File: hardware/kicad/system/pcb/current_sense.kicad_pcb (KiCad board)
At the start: 2 copper layers, 134 x 58 mm, 17 parts, among them J1 kanal 1 retur, J2 kanal 2 retur, J3 kanal 3 retur, J4 Arduino, U1 LM358, U2 LM358

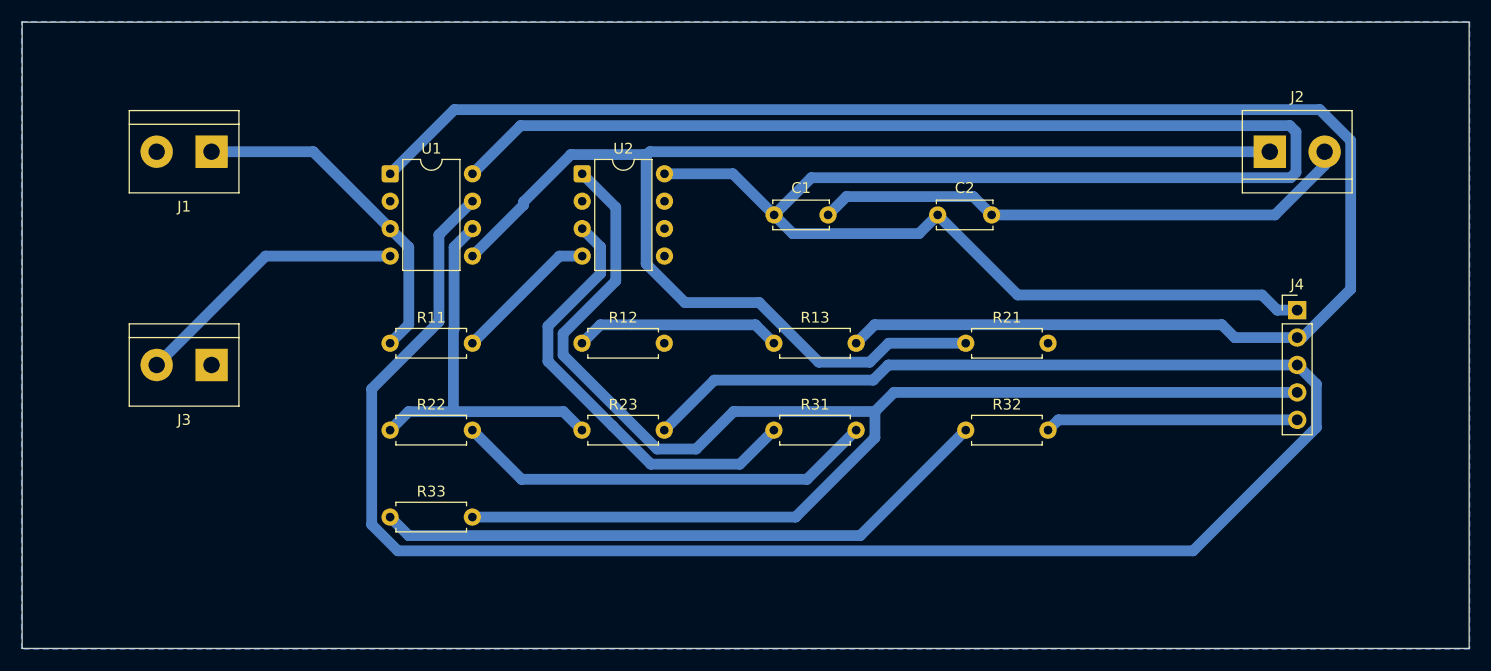
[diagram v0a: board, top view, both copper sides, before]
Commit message: Apply fiber-laser design rules from the DTU-PCB-prototyping guide
All seven boards rebuilt to meet the XTool fiber laser workflow
(SimsesLab/DTU-PCB-prototyping): 1.0 mm tracks, 0.8 mm clearance, solid
no-net fill zone on B.Cu (pad connection: none) so the laser only
engraves the isolation channels, DIP footprints switched to the
_LongPads variants from the guide's shop table.

TO packages cannot meet 0.8 mm pad-to-pad at stock sizes, so
energy_system.pretty now has TO-220-3_Vertical_LaserPads (pads narrowed
to 1.7 mm -> 0.84 mm gap; make_laserpads.py regenerates). The MPPT pass
transistor moves BD139 -> TIP41A (shop part): TO-126's 2.28 mm pitch can
never satisfy the rule, and TO-220 handles the ~7 W better anyway.

Two more bugs caught in this pass:
- Device:Q_NMOS uses letter pin numbers (G/D/S) while TO-220 pads are
  1/2/3 - buck/boost MOSFET pads silently got NO net in the earlier
  boards (no-net pads don't count as unconnected). pcb_build.py now maps
  G/D/S->1/2/3 and fails hard if a component ends up netless.
- DRC now 0 violations on all seven boards; remaining airwires are the
  documented jumpers.
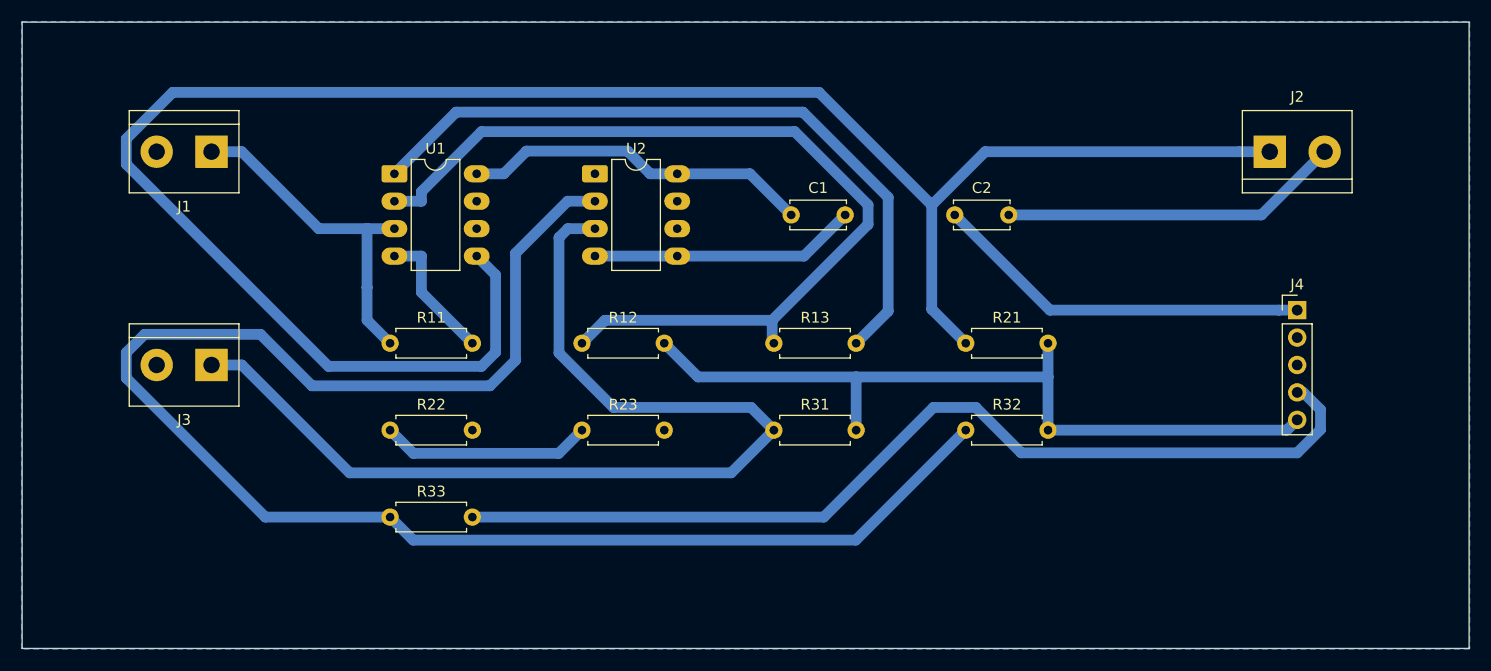
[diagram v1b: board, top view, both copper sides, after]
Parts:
- U1, U2: footprint DIP-8_W7.62mm -> DIP-8_W7.62mm_LongPads
- moved C1 1.58 mm to (91.2, 37.9)
- moved C2 1.58 mm to (106.4, 37.9)
- moved U2 1.18 mm to (73.0, 34.0)
- moved U1 0.39 mm to (54.5, 34.0)
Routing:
- net /I_SENSE2: track 194.7 -> 0.00 mm
- net +5V: track 197.3 -> 67.8 mm
- net /FB3: track 58.1 -> 149.5 mm
- net /I_SENSE1: track 155.2 -> 66.1 mm
- net /FB1: track 19.2 -> 84.9 mm
- net /RET2: track 122.2 -> 182.6 mm
- net /RET3: track 41.2 -> 95.1 mm
- net /I_SENSE3: track 136.6 -> 90.0 mm
- net /FB2: track 36.9 -> 19.6 mm
- net GND: track 152.7 -> 142.2 mm
- added copper zone on B.Cu, net (none)
- removed copper zone on B.Cu, net GND

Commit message: Engrave component references into the copper on all boards
The fiber laser has no silkscreen step, so the refdes (R1, U1, ...) are
placed as mirrored copper text on B.Cu next to each component - they
engrave in the same run as the traces and read correctly from the
solder side. Placement is collision-checked against tracks/pads/other
text (copper text over a track would short or sever it); tracks are
sampled into small boxes so diagonal runs don't false-positive. 86 of
96 labels fit; the handful dropped in dense spots are listed in
production/README.md and still appear on the F_Fab plots.

Also exports <board>_silk_top.dxf (F.Silkscreen + outline) per board as
an optional top-side engraving pass - run it on the component side
BEFORE the copper run, and do NOT mirror that one.

DRC still 0 violations on all seven; jumper lists updated.
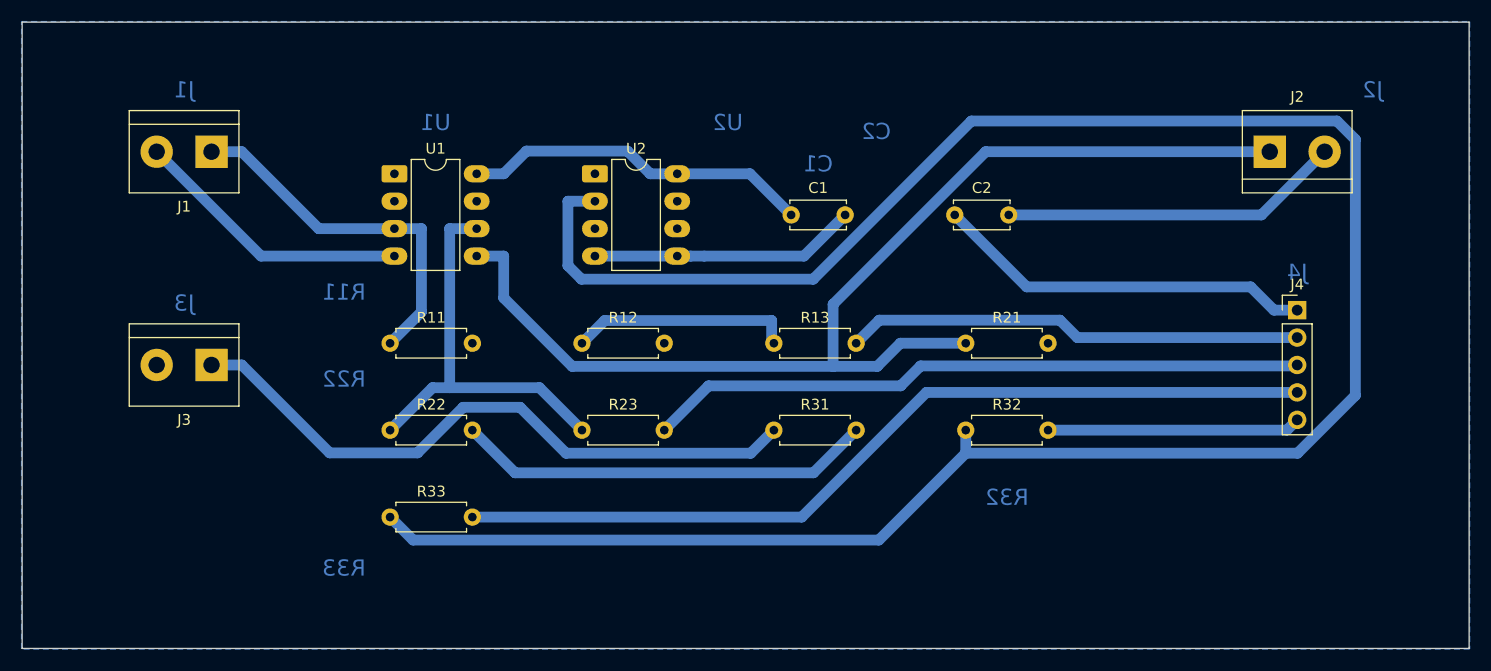
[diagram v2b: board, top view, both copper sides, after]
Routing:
- net /RET2: track 182.6 -> 104.7 mm
- net /FB1: track 84.9 -> 20.6 mm
- net /I_SENSE2: track 0.00 -> 61.1 mm
- net /FB3: track 149.5 -> 210.3 mm
- net /RET3: track 95.1 -> 59.8 mm
- net /I_SENSE1: track 66.1 -> 42.4 mm
- net /FB2: track 19.6 -> 38.3 mm
- net /I_SENSE3: track 90.0 -> 81.2 mm
- net /RET1: track 31.4 -> 34.2 mm
- net GND: track 142.2 -> 144.7 mm
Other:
- board text added: "C1"
- board text added: "C2"
- board text added: "J1"
- board text added: "J2"
- board text added: "J3"
- board text added: "J4"
- board text added: "R11"
- board text added: "R22"
- board text added: "R32"
- board text added: "R33"
- board text added: "U1"
- board text added: "U2"
